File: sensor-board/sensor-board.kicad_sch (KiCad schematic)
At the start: 102 parts, among them J1 USB_C_Receptacle_USB2.0_16P, J10 cap3, J11 cap4, J2 Conn_01x06, J3 aux pwr, J4 SWD, J5 water 1, J6 water 2, J7 relay, J8 cap1, J9 cap2, K1 SIL03-1A72-71D, Q1 Si2312, Q2 Si2312, SW1 SW_Push, U1 MLPF-WB55-01E3, U10 EKMB130711, U11 DRV5032, U2 STM32WB55CCUx, U3 MCP1703Ax-300xxTT, U4 SHT40-AD1F-R2, U5 VL53L1CXV0FY1, U6 TLV4082, U7 CLS16D24-44, U8 LIS2DE12TR, U9 FDC2114RGHR, Y1 32MHz, Y2 32.768KHz

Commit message: prepare production files
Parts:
- added H1, H2: MountingHole, MountingHole:MountingHole_2.2mm_M2, symbol Mechanical:MountingHole
- AE1, BT1, K1, MIC1, TP1, TP2, TP3, TP4, TP5, TP6, TP7, TP8, U10, U4, U5, U7, U8, U9: now left out of the parts list
- C1, C14, C19, C20, C29: KiLib_Generator (none) -> SMD_2terminal_chip_molded; LCSC (none) -> C23733
- C10: KiLib_Generator (none) -> SMD_2terminal_chip_molded; LCSC (none) -> C1546
- C11: value 4.7uf -> 4.7uF; footprint Capacitor_SMD:C_0402_1005Metric -> Capacitor_SMD:C_0805_2012Metric; KiLib_Generator (none) -> SMD_2terminal_chip_molded; LCSC (none) -> C1779
- C12, C15, C16, C17, C18, C2, C21, C22, C23, C30, C31, C4, C6, C7, C9: KiLib_Generator (none) -> SMD_2terminal_chip_molded; LCSC (none) -> C141382
- C13: value 4.7uf -> 4.7uF; KiLib_Generator (none) -> SMD_2terminal_chip_molded; LCSC (none) -> C23733
- C24, C32: KiLib_Generator (none) -> SMD_2terminal_chip_molded; LCSC (none) -> C52923
- C25, C26, C27, C28: KiLib_Generator (none) -> SMD_2terminal_chip_molded; LCSC (none) -> C1562
- C3, C5, L1, L2, L3, L4, L5, L6: KiLib_Generator (none) -> SMD_2terminal_chip_molded
- C8: value 1.0uF -> 1uF; KiLib_Generator (none) -> SMD_2terminal_chip_molded; LCSC (none) -> C52923
- D1: KiLib_Generator (none) -> SMD_2terminal_chip_molded; LCSC (none) -> C84256
- D2: LCSC (none) -> C2128
- J10, J11, J3, J5, J6, J7, J8, J9: KiLib_Generator (none) -> connector/SMD_single_row_plus_mounting_pad; now left out of the parts list
- J2: KiLib_Generator (none) -> connector/pin_header_socket; now left out of the parts list
- Q1, Q2: symbol Simulation_SPICE:NMOS -> Transistor_FET:Q_NMOS_GSD; KiLib_Generator (none) -> package/gullwing
- R1: value 1K -> 1k; KiLib_Generator (none) -> SMD_2terminal_chip_molded; LCSC (none) -> C11702
- R10, R11, R15, R16, R20, R21: KiLib_Generator (none) -> SMD_2terminal_chip_molded; LCSC (none) -> C11702
- R12, R19: value 1.0k -> 1k; KiLib_Generator (none) -> SMD_2terminal_chip_molded; LCSC (none) -> C11702
- R13, R14: KiLib_Generator (none) -> SMD_2terminal_chip_molded; LCSC (none) -> C26083
- R17: KiLib_Generator (none) -> SMD_2terminal_chip_molded; LCSC (none) -> C25741
- R18: KiLib_Generator (none) -> SMD_2terminal_chip_molded; LCSC (none) -> C22938
- R2, R6, R7, R8: KiLib_Generator (none) -> SMD_2terminal_chip_molded; LCSC (none) -> C25744
- R3, R9: value 10K -> 10k; KiLib_Generator (none) -> SMD_2terminal_chip_molded; LCSC (none) -> C25744
- R4, R5: KiLib_Generator (none) -> SMD_2terminal_chip_molded; LCSC (none) -> C25905
- SW1: LCSC (none) -> C720477
- U1: LCSC (none) -> C2651048
- U11, U6: KiLib_Generator (none) -> package/gullwing; now left out of the parts list
- U2: KiLib_Generator (none) -> package/no_lead; LCSC (none) -> C404023
- U3: KiLib_Generator (none) -> package/gullwing; LCSC (none) -> C625372
- Y1: KiLib_Generator (none) -> crystal_resonator_oscillator
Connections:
- net GND: now also Q1.2 (S), Q2.2 (S); no longer Q1.3 (S), Q2.3 (S)
- net at BT1.2 (-), J3.2 (Pin_2): now also Q1.3 (D); no longer Q1.1 (D)
- net at R19.1: now also Q1.1 (G); no longer Q1.2 (G)
- net at D2.2 (A), K1.5: now also Q2.3 (D); no longer Q2.1 (D)
- net at R12.2: now also Q2.1 (G); no longer Q2.2 (G)

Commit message: final fabricated board
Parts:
- C11: LCSC C1779 -> C23733
- C8: value 1uF -> 1.0uF
- H1, H2: KiLib_Generator mounting_hardware/mounting_hole -> (none)
- R1: value 1k -> 1K
- R12, R19: value 1k -> 1.0k
- R3, R9: value 10k -> 10K
- Y1: symbol Device:Crystal_GND2_Small -> Device:Crystal_GND24_Small
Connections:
- net GND: now also Y1.4 (G)
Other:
- moved on the sheet: C15

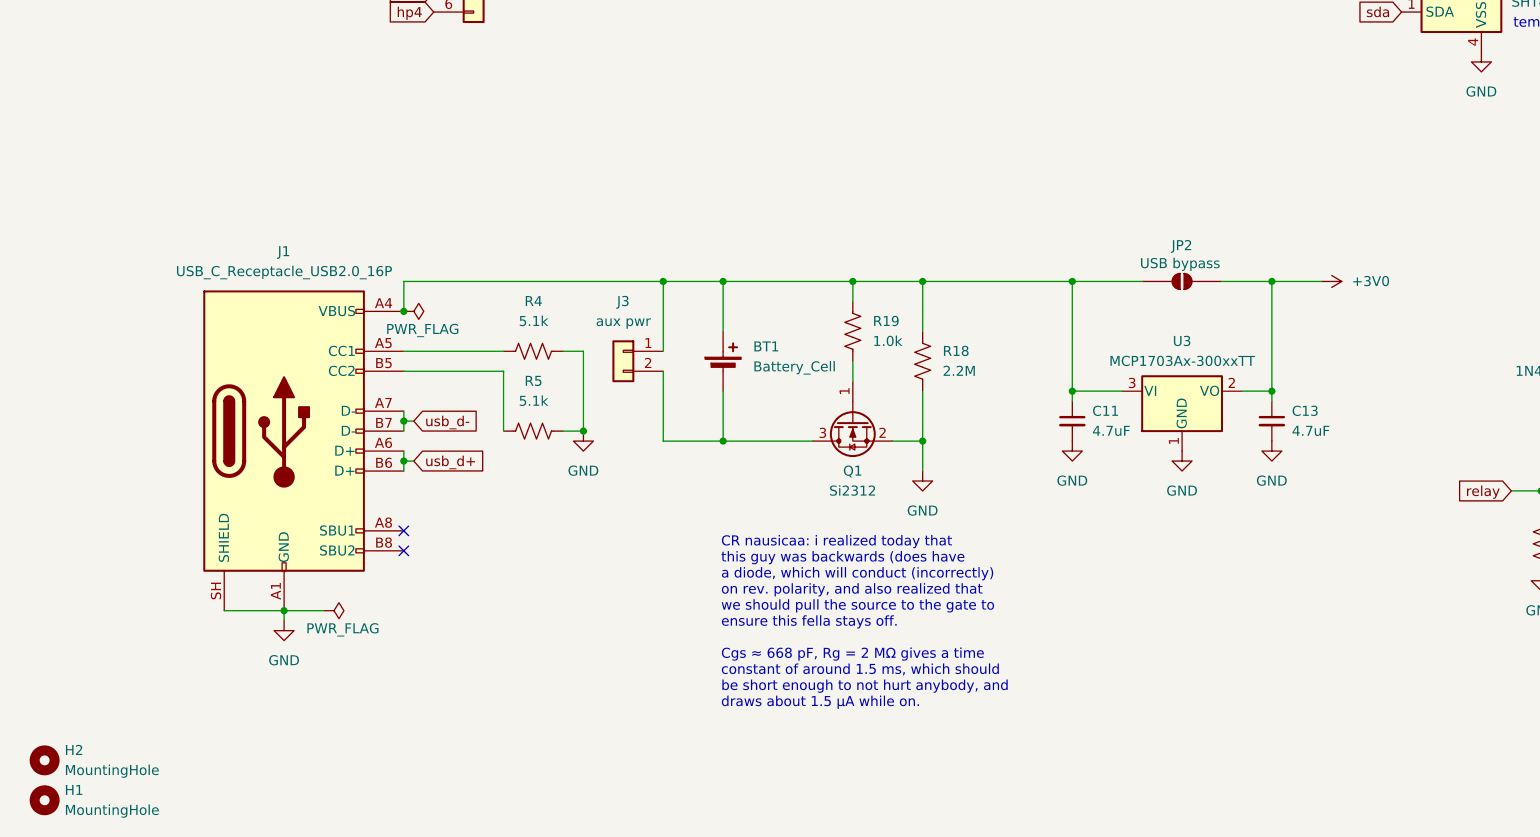
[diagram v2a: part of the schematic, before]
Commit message: [wip] new power supply circuits
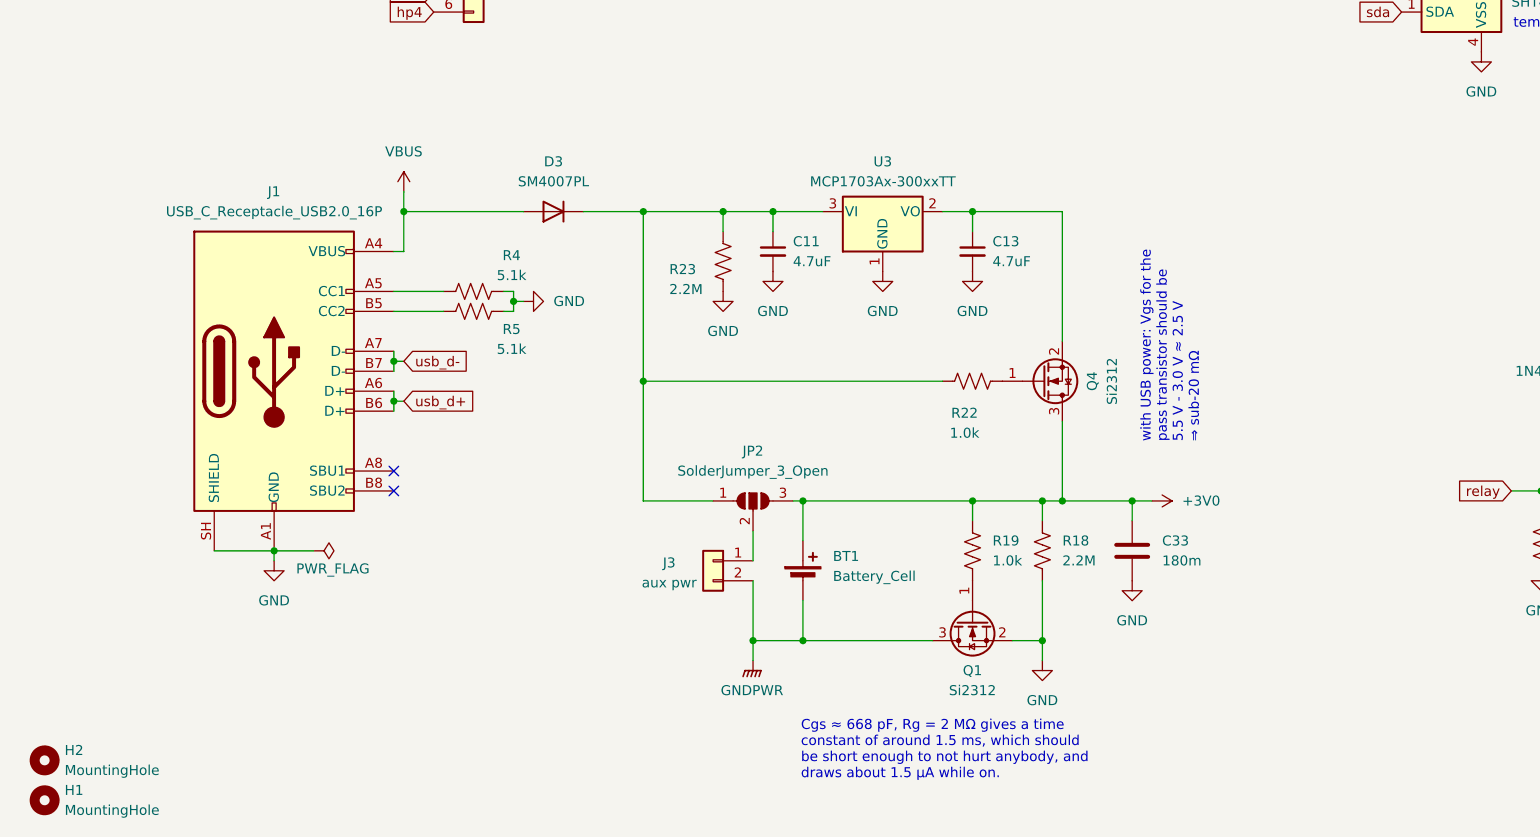
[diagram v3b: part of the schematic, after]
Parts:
- removed JP2: USB bypass, Jumper:SolderJumper-2_P1.3mm_Open_RoundedPad1.0x1.5mm, symbol Jumper:SolderJumper_2_Open
- added C33: 180m, Connector_PinHeader_2.54mm:PinHeader_1x02_P2.54mm_Vertical, symbol Device:C
- added D3: SM4007PL, Diode_SMD:D_SMA, symbol Device:D
- added JP2: SolderJumper_3_Open, Jumper:SolderJumper-3_P1.3mm_Open_RoundedPad1.0x1.5mm, symbol Jumper:SolderJumper_3_Open
- added Q4: Si2312, Package_TO_SOT_SMD:SOT-23, symbol Transistor_FET:Q_NMOS_GSD
- added R22: 1.0k, Resistor_SMD:R_0402_1005Metric, symbol Device:R_US
- added R23: 2.2M, Resistor_SMD:R_0603_1608Metric, symbol Device:R_US
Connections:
- net +3V0: now also BT1.1 (+), R18.1, R19.2, C33.1, JP2.3 (B), Q4.3 (D); no longer C13.1, U3.2 (VO)
- net GND: now also C33.2, R23.2
- net GNDPWR: now reaches BT1.2 (-), J3.2 (Pin_2), Q1.3 (D)
- new net: C11.1, D3.1 (K), JP2.1 (A), R22.1, R23.1, U3.3 (VI)
- new net: C13.1, Q4.2 (S), U3.2 (VO)
- new net: Q4.1 (G), R22.2
- new net: J3.1 (Pin_1), JP2.2 (C)
- new net VBUS: D3.2 (A), J1.A4 (VBUS), J1.A9 (VBUS), J1.B4 (VBUS), J1.B9 (VBUS)
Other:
- note added: "Cgs ≈ 668 pF, Rg = 2 MΩ gives a time constant of around 1.5 ms, which should be short enough to not hurt anybody, and draws about 1.5 μA while on."
- note added: "with USB power: Vgs for the pass transistor should be 5.5 V - 3.0 V ≈ 2.5 V ⇒ sub-20 mΩ"
- note removed: "CR nausicaa: i realized today that this guy was backwards (does have a diode, which will conduct (incorrectly) on rev. polarity, and also realized that we should pull the source to the gate to ensure this fella stays off. Cgs ≈ 668 pF, Rg = 2 MΩ gives a time constant of around 1.5 ms, which should be short enough to not hurt anybody, and draws about 1.5 μA while on."
- moved on the sheet: BT1, C11, C13, J1, J3, Q1, R18, R19, R4, R5, U3
